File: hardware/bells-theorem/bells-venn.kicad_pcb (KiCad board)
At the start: 2 copper layers, 257.4 x 128.5 mm, 340 parts, among them J1 Conn_02x05_Odd_Even, J10 D, J11 C, J12 DA, J13 CD, J14 DAB, J15 CDA, J16 A, J17 B, J18 AB, J19 BC, J2 left, J20 ABC, J21 BCD, J22 left, J23 right, J3 right, J4 IN, J5 CVA, J6 CVB, J7 CVC, J8 CVD, J9 ABCD, Q1 2N3904, Q10 2N3904, Q11 2N3904, Q12 2N3904, Q13 2N3904, Q2 2N3904, Q3 2N3904, Q4 2N3904, Q5 2N3904, Q6 2N3904, Q7 2N3904, Q8 2N3904, Q9 2N3904, U1 Teensy4.1, U10 TL074, U19 TL074, U2 L78L05_TO92, U20 TL074, U21 TL072, U3 L78L33_TO92, U4 TL074, U5 TL074, U6 TL074, U7 TL072, U8 TL074, U9 TL074

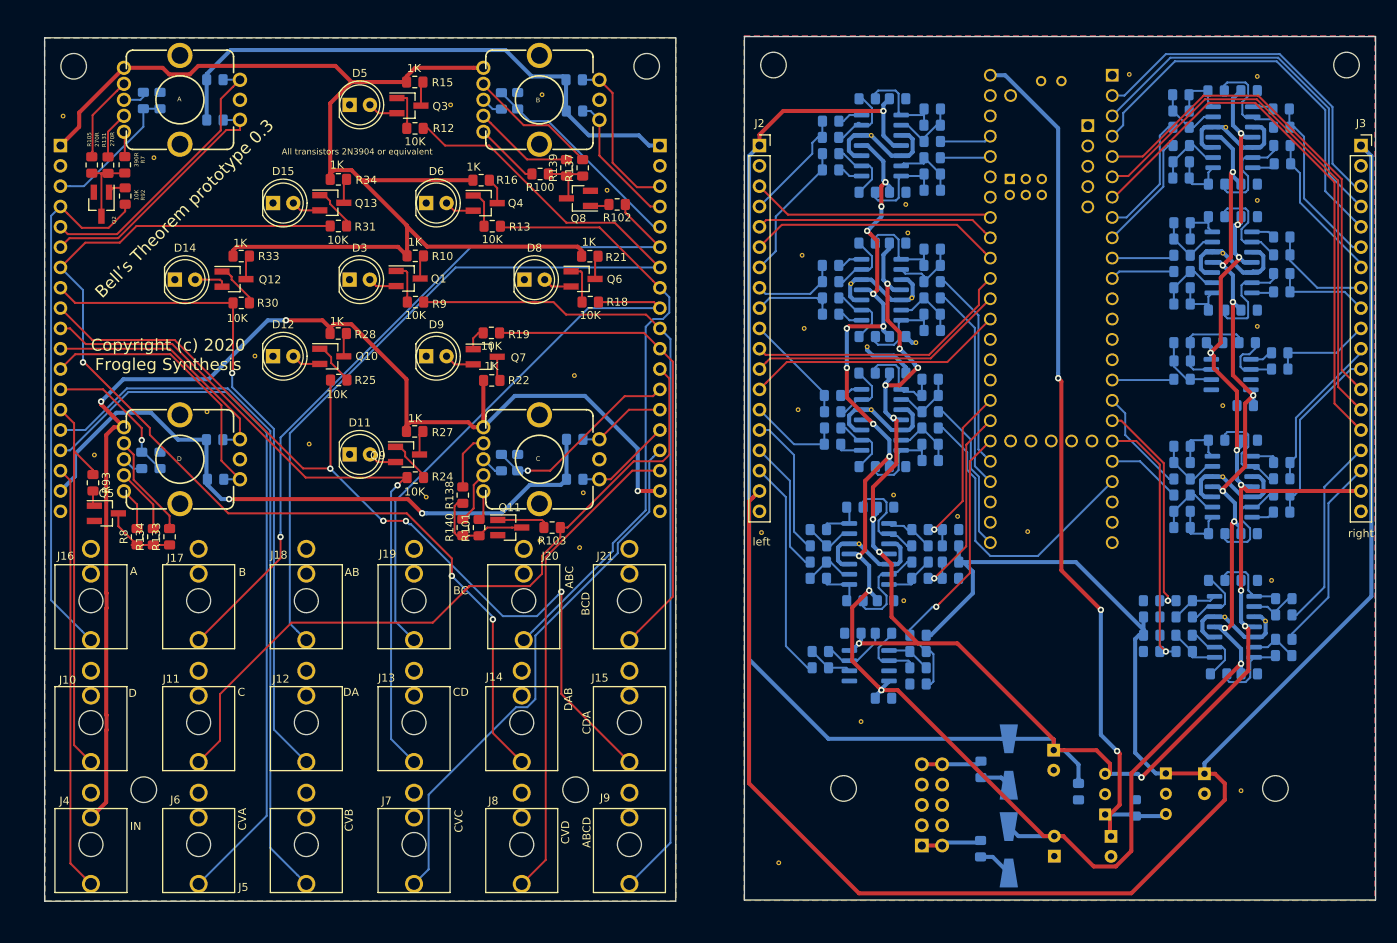
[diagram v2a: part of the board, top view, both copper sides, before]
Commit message: version 0.3, update for corrected LED drivers, other tweaks
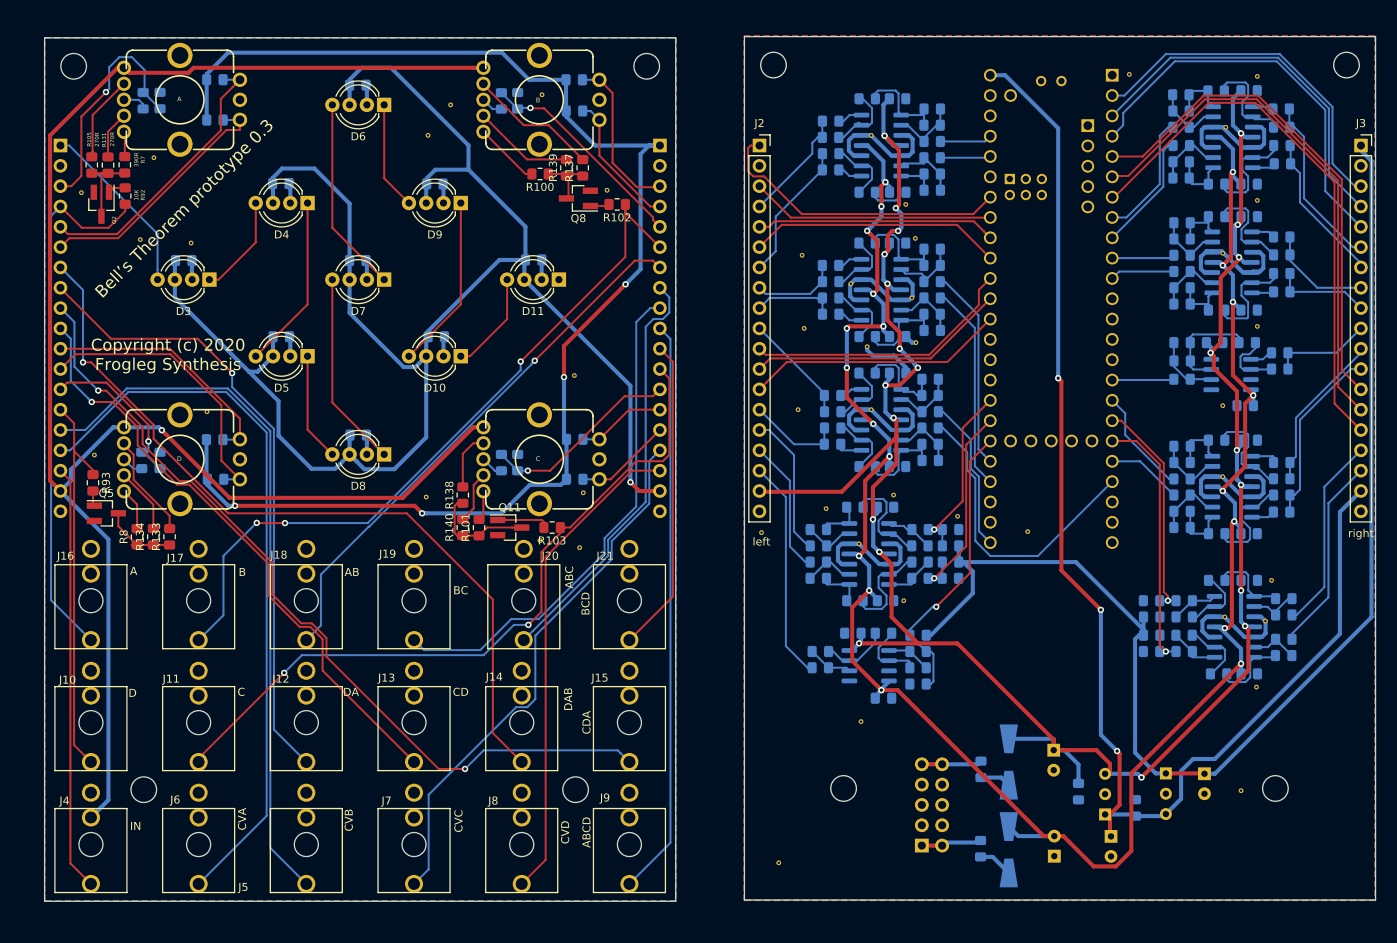
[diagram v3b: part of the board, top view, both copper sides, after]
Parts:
- removed D12, D14, D15: LED_Small_ALT, LED_THT:LED_D5.0mm_Clear
- removed Q1, Q10, Q12, Q13, Q3, Q4, Q6, Q7, Q9: 2N3904, Package_TO_SOT_SMD:SOT-23_Handsoldering
- removed R10, R15, R16, R21, R22, R27, R28, R33, R34: 1K, Resistor_SMD:R_0805_2012Metric_Pad1.15x1.40mm_HandSolder
- removed R12, R13, R18, R19, R24, R25, R30, R31, R9: 10K, Resistor_SMD:R_0805_2012Metric_Pad1.15x1.40mm_HandSolder
- removed the REF** at (144.4, 78.7)
- removed the REF** at (137.6, 67.7)
- added C40: C_Small, Capacitor_SMD:C_0805_2012Metric_Pad1.15x1.40mm_HandSolder, B.Cu at (140.8, 46.2)
- added C41: C_Small, Capacitor_SMD:C_0805_2012Metric_Pad1.15x1.40mm_HandSolder, B.Cu at (140.9, 65.3)
- added C42: C_Small, Capacitor_SMD:C_0805_2012Metric_Pad1.15x1.40mm_HandSolder, B.Cu at (150.5, 33.9)
- added C43: C_Small, Capacitor_SMD:C_0805_2012Metric_Pad1.15x1.40mm_HandSolder, B.Cu at (128.7, 55.8)
- added C44: C_Small, Capacitor_SMD:C_0805_2012Metric_Pad1.15x1.40mm_HandSolder, B.Cu at (150.5, 55.8)
- added C45: C_Small, Capacitor_SMD:C_0805_2012Metric_Pad1.15x1.40mm_HandSolder, B.Cu at (160.3, 65.3)
- added C46: C_Small, Capacitor_SMD:C_0805_2012Metric_Pad1.15x1.40mm_HandSolder, B.Cu at (172.4, 55.7)
- added C47: C_Small, Capacitor_SMD:C_0805_2012Metric_Pad1.15x1.40mm_HandSolder, B.Cu at (160.1, 46.2)
- added C48: C_Small, Capacitor_SMD:C_0805_2012Metric_Pad1.15x1.40mm_HandSolder, B.Cu at (150.5, 77.6)
- added D10: BCD, LED_THT:LED_D5.0mm-4_RGB_Wide_Pins, F.Cu at (163.3, 67.7)
- added D4: DAB, LED_THT:LED_D5.0mm-4_RGB_Wide_Pins, F.Cu at (144.2, 48.6)
- added D7: ABCD, LED_THT:LED_D5.0mm-4_RGB_Wide_Pins, F.Cu at (153.7, 58.2)
- added REF**: stitch-via-0.6mm, My Library:stitch-via-0.6mm, F.Cu at (209.0, 86.8)
- added REF**: stitch-via-0.6mm, My Library:stitch-via-0.6mm, F.Cu at (262.8, 109.1)
- added REF**: stitch-via-0.6mm, My Library:stitch-via-0.6mm, F.Cu at (159.2, 40.1)
- added REF**: stitch-via-0.6mm, My Library:stitch-via-0.6mm, F.Cu at (129.6, 53.6)
- added REF**: stitch-via-0.6mm, My Library:stitch-via-0.6mm, F.Cu at (123.3, 53.2)
- D11: value LED_Small_ALT -> BC; footprint LED_THT:LED_D5.0mm_Clear -> LED_THT:LED_D5.0mm-4_RGB_Wide_Pins
- D3: value LED_Small_ALT -> DA; footprint LED_THT:LED_D5.0mm_Clear -> LED_THT:LED_D5.0mm-4_RGB_Wide_Pins
- D5: value LED_Small_ALT -> CDA; footprint LED_THT:LED_D5.0mm_Clear -> LED_THT:LED_D5.0mm-4_RGB_Wide_Pins
- D6: value LED_Small_ALT -> AB; footprint LED_THT:LED_D5.0mm_Clear -> LED_THT:LED_D5.0mm-4_RGB_Wide_Pins
- D8: value LED_Small_ALT -> CD; footprint LED_THT:LED_D5.0mm_Clear -> LED_THT:LED_D5.0mm-4_RGB_Wide_Pins
- D9: value LED_Small_ALT -> ABC; footprint LED_THT:LED_D5.0mm_Clear -> LED_THT:LED_D5.0mm-4_RGB_Wide_Pins
- moved D11 34.1 mm to (175.6, 58.2), turned to 180 degrees
- moved D5 31.9 mm to (144.2, 67.7), turned to 180 degrees
- moved D8 28.0 mm to (153.7, 80.0), turned to 180 degrees
- moved D9 19.6 mm to (163.3, 48.6), turned to 180 degrees
- moved D3 17.5 mm to (131.9, 58.2), turned to 180 degrees
- moved D6 13.3 mm to (153.7, 36.3), turned to 180 degrees
- moved REF** 9.84 mm to (115.9, 47.3)
- moved REF** 1.16 mm to (220.1, 53.0)
- turned R104 to 90 degrees
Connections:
- D11 pad 1: GND -> Net-(D11-Pad1)
- D11 pad 2: Net-(D11-Pad2) -> GND
- D3 pad 1: GND -> Net-(D3-Pad1)
- D3 pad 2: Net-(D3-Pad2) -> GND
- D5 pad 1: GND -> Net-(D5-Pad1)
- D5 pad 2: Net-(D5-Pad2) -> GND
- D6 pad 1: GND -> Net-(D6-Pad1)
- D6 pad 2: Net-(D6-Pad2) -> GND
- D8 pad 1: GND -> Net-(D7-Pad4)
- D8 pad 2: Net-(D8-Pad2) -> GND
- D9 pad 1: GND -> Net-(D10-Pad4)
- D9 pad 2: Net-(D9-Pad2) -> GND
- J2 pad 1: +12V -> /main/np_ctl
- J2 pad 18: +3V3 -> +12V
- J22 pad 1: +12V -> /main/np_ctl
- J22 pad 18: +3V3 -> +12V
- J23 pad 18: +12V -> +5V
- J3 pad 18: +12V -> +5V
- U1 pad 42: Net-(U1-Pad42) -> /main/np_ctl
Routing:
- net +5V: track 110.7 -> 379.1 mm, vias 3 -> 4
- net +12V: track 687.0 -> 495.8 mm, vias 21 -> 22
- net +3V3: track 424.8 -> 330.9 mm, vias 2 -> 4
- net /main/np_ctl: track 0.00 -> 60.2 mm
- net /main/AB: track 137.2 -> 86.9 mm, vias 0 -> 1
- net /main/DAB: track 152.2 -> 116.9 mm, vias 3 -> 1
- net /main/ABCD: track 115.4 -> 84.5 mm
- net Net-(D7-Pad4): track 0.00 -> 24.5 mm
- net Net-(D6-Pad4): track 0.00 -> 24.5 mm
- net /main/ABC: track 89.1 -> 66.0 mm
- net GND: track 133.8 -> 155.9 mm
- net Net-(D4-Pad1): track 0.00 -> 21.8 mm
- net Net-(D10-Pad4): track 0.00 -> 21.8 mm
- net /main/BCD: track 80.1 -> 59.3 mm
- net Net-(D5-Pad1): track 0.00 -> 13.6 mm
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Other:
- board text removed: "All transistors 2N3904 or equivalent"
- board text removed: "Bell’s Theorem prototype 0.2"

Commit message: modified for Kicad 6 updated testing code
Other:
- net class Default removed
- net class power removed

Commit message: Modified with Jim M's recommendations for input scaling
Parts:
- removed C6: 1uF, Capacitor_THT:CP_Radial_D5.0mm_P2.50mm
- added C49: 15p, Capacitor_SMD:C_0805_2012Metric_Pad1.18x1.45mm_HandSolder, B.Cu at (221.2, 97.5)
- added C50: 15p, Capacitor_SMD:C_0805_2012Metric_Pad1.18x1.45mm_HandSolder, B.Cu at (220.7, 87.3)
- added C51: 15p, Capacitor_SMD:C_0805_2012Metric_Pad1.18x1.45mm_HandSolder, B.Cu at (224.6, 106.0)
- added C52: 15p, Capacitor_SMD:C_0805_2012Metric_Pad1.18x1.45mm_HandSolder, B.Cu at (251.7, 106.8)
- added C53: 15p, Capacitor_SMD:C_0805_2012Metric_Pad1.18x1.45mm_HandSolder, B.Cu at (251.7, 96.2)
- added U11: SN74LV1T34DBV, Package_TO_SOT_SMD:SOT-23-5, B.Cu at (225.7, 33.8)
- C3: value 100nF -> 1uF; footprint Capacitor_SMD:C_0805_2012Metric_Pad1.15x1.40mm_HandSolder -> Capacitor_THT:CP_Radial_D5.0mm_P2.50mm
- C40, C41, C42, C43, C44, C45, C46, C47, C48: value C_Small -> 100nF
- D1, D2: value D_Schottky -> CDBM140-G
- L1, L2: value Ferrite_Bead_Small -> BLM21PG220SH1D
- R100, R101, R7, R8: value 390R -> 360R
- R102, R103, R92, R93: value 10K -> 15K
- R106, R107, R116, R117, R118: value 30K -> 100K
- R108, R109, R119, R120, R121: value 10K -> 33K
- R114, R115, R128, R129, R130: value 10K -> 220R
- U2: value L78L05_TO92 -> R-78B5.0-2.0; footprint Package_TO_SOT_THT:TO-92_Inline_Wide -> Converter_DCDC:Converter_DCDC_RECOM_R-78B-2.0_THT
- U3: value L78L33_TO92 -> MCP6002-xSN; footprint Package_TO_SOT_THT:TO-92_Inline_Wide -> Package_SO:SOIC-8_3.9x4.9mm_P1.27mm
- moved U3 25.2 mm to (235.3, 100.6), turned to 0 degrees
- moved C3 9.64 mm to (256.3, 120.0), turned to -90 degrees
- moved U2 5.03 mm to (243.9, 120.0), turned to -90 degrees
- moved C2 2.77 mm to (244.0, 130.5)
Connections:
- C3 pad 1: +5V -> +3V3
- D11 pad 1: Net-(D11-Pad1) -> unconnected-(D11-Pad1)
- D16 pad 2: /main/scaleright/CVC_out -> Net-(D16-Pad2)
- D17 pad 1: /main/scaleright/CVC_out -> Net-(D16-Pad2)
- D18 pad 2: /main/scaleright/CVD_out -> Net-(D18-Pad2)
- D19 pad 1: /main/scaleright/CVD_out -> Net-(D18-Pad2)
- D20 pad 2: /main/scaleleft/CVB_out -> Net-(D20-Pad2)
- D21 pad 1: /main/scaleleft/CVB_out -> Net-(D20-Pad2)
- D22 pad 2: /main/scaleleft/IN_out -> Net-(D22-Pad2)
- D23 pad 1: /main/scaleleft/IN_out -> Net-(D22-Pad2)
- D24 pad 2: /main/scaleleft/CVA_out -> Net-(D24-Pad2)
- D25 pad 1: /main/scaleleft/CVA_out -> Net-(D24-Pad2)
- D3 pad 4: /main/np_ctl -> Net-(D3-Pad4)
- J10 pad 2: Net-(J10-Pad2) -> unconnected-(J10-Pad2)
- J11 pad 2: Net-(J11-Pad2) -> unconnected-(J11-Pad2)
- J12 pad 2: Net-(J12-Pad2) -> unconnected-(J12-Pad2)
- J13 pad 2: Net-(J13-Pad2) -> unconnected-(J13-Pad2)
- J14 pad 2: Net-(J14-Pad2) -> unconnected-(J14-Pad2)
- J15 pad 2: Net-(J15-Pad2) -> unconnected-(J15-Pad2)
- J16 pad 2: Net-(J16-Pad2) -> unconnected-(J16-Pad2)
- J17 pad 2: Net-(J17-Pad2) -> unconnected-(J17-Pad2)
- J18 pad 2: Net-(J18-Pad2) -> unconnected-(J18-Pad2)
- J19 pad 2: Net-(J19-Pad2) -> unconnected-(J19-Pad2)
- J20 pad 2: Net-(J20-Pad2) -> unconnected-(J20-Pad2)
- J21 pad 2: Net-(J21-Pad2) -> unconnected-(J21-Pad2)
- J9 pad 2: Net-(J9-Pad2) -> unconnected-(J9-Pad2)
- R108 pad 1: Net-(R108-Pad1) -> Net-(D16-Pad2)
- R109 pad 1: Net-(R109-Pad1) -> Net-(D18-Pad2)
- R110 pad 2: Net-(R108-Pad1) -> Net-(D16-Pad2)
- R111 pad 2: Net-(R109-Pad1) -> Net-(D18-Pad2)
- R119 pad 1: Net-(R119-Pad1) -> Net-(D20-Pad2)
- R120 pad 1: Net-(R120-Pad1) -> Net-(D22-Pad2)
- R121 pad 1: Net-(R121-Pad1) -> Net-(D24-Pad2)
- R122 pad 2: Net-(R119-Pad1) -> Net-(D20-Pad2)
- R123 pad 2: Net-(R121-Pad1) -> Net-(D24-Pad2)
- R124 pad 2: Net-(R120-Pad1) -> Net-(D22-Pad2)
- U1 pad 12: Net-(U1-Pad12) -> unconnected-(U1-Pad12)
- U1 pad 13: Net-(U1-Pad13) -> unconnected-(U1-Pad13)
- U1 pad 14: Net-(U1-Pad14) -> unconnected-(U1-Pad14)
- U1 pad 15: Net-(U1-Pad15) -> unconnected-(U1-Pad15)
- U1 pad 22: Net-(U1-Pad22) -> unconnected-(U1-Pad22)
- U1 pad 23: Net-(U1-Pad23) -> unconnected-(U1-Pad23)
- U1 pad 24: Net-(U1-Pad24) -> unconnected-(U1-Pad24)
- U1 pad 26: Net-(U1-Pad26) -> unconnected-(U1-Pad26)
- U1 pad 27: Net-(U1-Pad27) -> unconnected-(U1-Pad27)
- U1 pad 33: Net-(U1-Pad33) -> unconnected-(U1-Pad33)
- U1 pad 35: Net-(U1-Pad35) -> unconnected-(U1-Pad35)
- U1 pad 42: /main/np_ctl -> Net-(U1-Pad42)
- U1 pad 43: Net-(U1-Pad43) -> unconnected-(U1-Pad43)
- U1 pad 49: Net-(U1-Pad49) -> unconnected-(U1-Pad49)
- U1 pad 50: Net-(U1-Pad50) -> unconnected-(U1-Pad50)
- U1 pad 51: Net-(U1-Pad51) -> unconnected-(U1-Pad51)
- U1 pad 52: Net-(U1-Pad52) -> unconnected-(U1-Pad52)
- U1 pad 53: Net-(U1-Pad53) -> unconnected-(U1-Pad53)
- U1 pad 54: Net-(U1-Pad54) -> unconnected-(U1-Pad54)
- U1 pad 55: Net-(U1-Pad55) -> unconnected-(U1-Pad55)
- U1 pad 56: Net-(U1-Pad56) -> unconnected-(U1-Pad56)
- U1 pad 57: Net-(U1-Pad57) -> unconnected-(U1-Pad57)
- U1 pad 58: Net-(U1-Pad58) -> unconnected-(U1-Pad58)
- U1 pad 59: Net-(U1-Pad59) -> unconnected-(U1-Pad59)
- U1 pad 60: Net-(U1-Pad60) -> unconnected-(U1-Pad60)
- U1 pad 61: Net-(U1-Pad61) -> unconnected-(U1-Pad61)
- U1 pad 62: Net-(U1-Pad62) -> unconnected-(U1-Pad62)
- U1 pad 63: Net-(U1-Pad63) -> unconnected-(U1-Pad63)
- U1 pad 64: Net-(U1-Pad64) -> unconnected-(U1-Pad64)
- U1 pad 65: Net-(U1-Pad65) -> unconnected-(U1-Pad65)
- U1 pad 66: Net-(U1-Pad66) -> unconnected-(U1-Pad66)
- U1 pad 67: Net-(U1-Pad67) -> unconnected-(U1-Pad67)
- U19 pad 1: Net-(R108-Pad1) -> Net-(D16-Pad2)
- U19 pad 7: Net-(R109-Pad1) -> Net-(D18-Pad2)
- U2 pad 1: +5V -> +12V
- U2 pad 3: +12V -> +5V
- U20 pad 14: Net-(R119-Pad1) -> Net-(D20-Pad2)
- U20 pad 8: Net-(R121-Pad1) -> Net-(D24-Pad2)
- U21 pad 7: Net-(R120-Pad1) -> Net-(D22-Pad2)
- U3 pad 2: GND -> +3V3
- U3 pad 3: +5V -> Net-(U1-Pad46)
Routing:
- net Net-(U1-Pad46): track 0.00 -> 71.7 mm, vias 0 -> 2
- net Net-(D18-Pad2): track 0.00 -> 44.4 mm, vias 0 -> 1
- net Net-(D22-Pad2): track 0.00 -> 42.5 mm, vias 0 -> 1
- net /main/scaleleft/IN_out: track 37.1 -> 0.00 mm, vias 1 -> 0
- net /main/scaleright/CVD_out: track 34.9 -> 0.00 mm, vias 1 -> 0
- net Net-(D24-Pad2): track 0.00 -> 32.2 mm, vias 0 -> 1
- net Net-(D20-Pad2): track 0.00 -> 28.6 mm, vias 0 -> 1
- net /main/scaleleft/CVA_out: track 26.4 -> 0.00 mm, vias 1 -> 0
- net /main/scaleleft/CVB_out: track 22.9 -> 0.00 mm, vias 1 -> 0
- net Net-(U1-Pad42): track 0.00 -> 18.3 mm
- net +5V: track 379.1 -> 394.4 mm
- net Net-(D16-Pad2): track 0.00 -> 11.7 mm
- net Net-(R108-Pad1): track 9.68 -> 0.00 mm
- net Net-(R109-Pad1): track 9.46 -> 0.00 mm
- net Net-(R120-Pad1): track 8.52 -> 0.00 mm
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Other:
- board text added: "Bell’s Theorem prototype 0.4"

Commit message: All changes up to date with latest revisions
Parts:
- removed C30, C31, C32, C34: 100nF, Capacitor_SMD:C_0805_2012Metric_Pad1.15x1.40mm_HandSolder
- removed D16, D17, D18, D19, D20, D21, D22, D23, D24, D25: D_Schottky, Resistor_SMD:R_0805_2012Metric_Pad1.15x1.40mm_HandSolder
- removed R106, R107: 100K, Resistor_SMD:R_0805_2012Metric_Pad1.15x1.40mm_HandSolder
- removed R108, R109: 33K, Resistor_SMD:R_0805_2012Metric_Pad1.15x1.40mm_HandSolder
- removed R110, R111, R112, R113, R122, R123, R124, R125, R126, R127: 10K, Resistor_SMD:R_0805_2012Metric_Pad1.15x1.40mm_HandSolder
- removed the REF** at (258.8, 100.3)
- removed the REF** at (217.4, 85.1)
- removed the REF** at (213.1, 91.2)
- removed the REF** at (218.7, 98.3)
- removed the REF** at (264.7, 95.8)
- removed the REF** at (263.9, 100.8)
- removed the REF** at (225.4, 87.8)
- removed the REF** at (209.0, 86.8)
- removed the REF** at (262.8, 109.1)
- removed U19, U20: TL074, Package_SO:SOIC-14_3.9x8.7mm_P1.27mm
- removed U21: TL072, Package_SO:SOIC-8_3.9x4.9mm_P1.27mm
- added ?: , , F.Cu at (273.8, 63.1)
- added ?: , , F.Cu at (219.1, 83.1)
- added ?: , , F.Cu at (212.9, 94.6)
- added ?: , , F.Cu at (264.2, 89.9)
- added R10: 20K, Resistor_SMD:R_0805_2012Metric_Pad1.20x1.40mm_HandSolder, B.Cu at (223.0, 91.9)
- added R12: 12K, Resistor_SMD:R_0805_2012Metric_Pad1.20x1.40mm_HandSolder, B.Cu at (223.0, 89.9)
- added R13: 100K, Resistor_SMD:R_0805_2012Metric_Pad1.20x1.40mm_HandSolder, B.Cu at (266.4, 100.3)
- added R15: 100K, Resistor_SMD:R_0805_2012Metric_Pad1.20x1.40mm_HandSolder, B.Cu at (254.0, 100.6)
- added R16: 33K, Resistor_SMD:R_0805_2012Metric_Pad1.20x1.40mm_HandSolder, B.Cu at (266.4, 98.0)
- added R18: 33K, Resistor_SMD:R_0805_2012Metric_Pad1.20x1.40mm_HandSolder, B.Cu at (254.0, 98.6)
- added R9: 470R, Resistor_SMD:R_0805_2012Metric_Pad1.20x1.40mm_HandSolder, B.Cu at (125.2, 52.8)
- added REF**: stitch-via-0.6mm, My Library:stitch-via-0.6mm, F.Cu at (262.9, 101.9)
- added U12: MCP6004, Package_SO:SO-14_3.9x8.65mm_P1.27mm, B.Cu at (216.9, 94.5)
- added U13: MCP6002-xSN, Package_SO:SOIC-8_3.9x4.9mm_P1.27mm, B.Cu at (260.2, 97.9)
- C1, C14, C15, C16, C17, C18, C19, C20, C21, C28, C29, C33, C35, C36, C37, C38, C39, C40, C41, C42, C43, C44, C45, C46, C47, C48: footprint Capacitor_SMD:C_0805_2012Metric_Pad1.15x1.40mm_HandSolder -> Capacitor_SMD:C_0805_2012Metric_Pad1.18x1.45mm_HandSolder
- C10, C11, C12, C13, C22, C23, C24, C25, C26, C27, C7, C8, C9: value 15nF -> 1nF; footprint Capacitor_SMD:C_0805_2012Metric_Pad1.15x1.40mm_HandSolder -> Capacitor_SMD:C_0805_2012Metric_Pad1.18x1.45mm_HandSolder
- C49, C50, C51, C52, C53: value 15p -> 1n
- R1, R100, R101, R102, R103, R104, R105, R11, R116, R117, R118, R119, R120, R121, R131, R132, R133, R134, R135, R136, R137, R138, R139, R14, R140, R17, R2, R20, R23, R26, R29, R3, R32, R35, R36, R37, R38, R39, R4, R40, R41, R42, R43, R44, R45, R46, R47, R48, R49, R5, R50, R51, R52, R53, R54, R55, R56, R57, R58, R59, R6, R60, R61, R62, R63, R64, R65, R66, R67, R68, R69, R7, R70, R71, R72, R73, R74, R75, R76, R77, R78, R79, R8, R80, R81, R82, R83, R84, R85, R86, R87, R88, R89, R90, R91, R92, R93, R94, R95, R96, R97, R98, R99: footprint Resistor_SMD:R_0805_2012Metric_Pad1.15x1.40mm_HandSolder -> Resistor_SMD:R_0805_2012Metric_Pad1.20x1.40mm_HandSolder
- R114, R115, R128, R129, R130: value 220R -> 22R; footprint Resistor_SMD:R_0805_2012Metric_Pad1.15x1.40mm_HandSolder -> Resistor_SMD:R_0805_2012Metric_Pad1.20x1.40mm_HandSolder
- U3: value MCP6002-xSN -> ADP150-3.3; footprint Package_SO:SOIC-8_3.9x4.9mm_P1.27mm -> Package_TO_SOT_SMD:TSOT-23-5
- moved U3 17.1 mm to (246.8, 113.3)
- moved C53 15.2 mm to (266.7, 93.5), turned to 0 degrees
- moved C33 13.1 mm to (222.8, 94.5), turned to 0 degrees
- moved R114 13.0 mm to (266.5, 95.8)
- moved C52 12.5 mm to (254.0, 94.5)
- moved R120 10.8 mm to (218.7, 101.8), turned to -90 degrees
- moved R129 10.8 mm to (210.9, 99.8)
- moved C50 9.92 mm to (210.8, 86.9)
- moved R128 9.91 mm to (210.8, 88.9)
- moved R118 9.50 mm to (216.4, 101.8), turned to -90 degrees
- moved C49 8.33 mm to (214.1, 101.9), turned to -90 degrees
- moved R115 8.13 mm to (254.0, 96.5), turned to 180 degrees
- moved C51 4.47 mm to (222.8, 101.9), turned to -90 degrees
- moved R121 3.62 mm to (210.8, 97.8)
- moved R117 3.49 mm to (210.9, 95.5)
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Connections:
- C29 pad 1: +12V -> +3V3
- C33 pad 1: +12V -> +3V3
- R119 pad 1: Net-(D20-Pad2) -> Net-(R119-Pad1)
- R120 pad 1: Net-(D22-Pad2) -> Net-(R120-Pad1)
- R121 pad 1: Net-(D24-Pad2) -> Net-(R121-Pad1)
- R128 pad 2: Net-(R125-Pad1) -> Net-(R119-Pad1)
- R129 pad 2: Net-(R127-Pad1) -> Net-(R121-Pad1)
- R130 pad 2: Net-(R126-Pad1) -> Net-(R120-Pad1)
- U1 pad 12: unconnected-(U1-Pad12) -> /main/3Venable
- U1 pad 46: Net-(U1-Pad46) -> unconnected-(U1-Pad46)
- U3 pad 1: +3V3 -> +5V
- U3 pad 2: +3V3 -> GND
- U3 pad 3: Net-(U1-Pad46) -> /main/3Venable
- U3 pad 4: GND -> unconnected-(U3-Pad4)
- U3 pad 5: Net-(U3-Pad5) -> +3V3
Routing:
- net Net-(U1-Pad46): track 71.7 -> 0.00 mm, vias 2 -> 0
- net /main/scaleleft/scaleRef: track 0.00 -> 63.7 mm, vias 0 -> 2
- net /main/3Venable: track 0.00 -> 56.2 mm, vias 0 -> 1
- net Net-(D18-Pad2): track 44.4 -> 0.00 mm, vias 1 -> 0
- net Net-(D22-Pad2): track 42.5 -> 0.00 mm, vias 1 -> 0
- net /main/scaleleft/CVA_out: track 0.00 -> 36.3 mm, vias 0 -> 1
- net Net-(D24-Pad2): track 32.2 -> 0.00 mm, vias 1 -> 0
- net /main/scaleleft/CVB_out: track 0.00 -> 30.1 mm, vias 0 -> 1
- net GND: track 155.9 -> 126.2 mm
- net Net-(D20-Pad2): track 28.6 -> 0.00 mm, vias 1 -> 0
- net /main/scaleleft/IN_out: track 0.00 -> 28.0 mm, vias 0 -> 1
- net /main/scaleright/CVD_out: track 0.00 -> 25.1 mm, vias 0 -> 1
- net -12V: track 260.8 -> 239.1 mm, vias 20 -> 16
- net +12V: track 495.8 -> 478.2 mm, vias 22 -> 17
- net /main/CVD: track 85.5 -> 100.2 mm
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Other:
- board text added: "Copyright (c) 2021 Frogleg Synthesis"
- board text added: "Thanks to Nyles Miszczyk for the inspiration to make this And Jim Matheson for much help with Teensy Interfacing"
- board text removed: ">"
- board text removed: "Copyright (c) 2020 Frogleg Synthesis"
- board text removed: "Thanks to Nyles Miszczyk for the inspiration to make this"
